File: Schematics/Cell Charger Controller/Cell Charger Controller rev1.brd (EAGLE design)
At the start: 177.8 x 114.3 mm, 54 parts, among them Q1 DMG3406L, U1 HM2102NLT

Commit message: charger controller board ready for review
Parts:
- added X1: CONNECTOR-4NANO-FIT-VERTICAL-4, HyTechDevices:1053101204
- moved C2 0.92 mm to (113.3, 79.0)
- moved R8 0.76 mm to (115.6, 26.2)
- moved C3 0.57 mm to (109.2, 79.0)
- moved U$5 0.57 mm to (119.4, 78.7)
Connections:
- net +12V: now also X1.1
- net ALERT_INA: now also U$2.A3
- net CANH: now also X1.4
- net CANL: now also X1.3
- net GND: now also X1.2
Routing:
- net ALERT_INA: track 0.00 -> 86.3 mm, vias 0 -> 2
- net +12V: track 18.0 -> 81.0 mm
- net CANL: track 0.00 -> 8.62 mm
- net CANH: track 0.00 -> 8.62 mm
- net +3V3: track 176.3 -> 178.2 mm
- net N$12: track 25.3 -> 26.7 mm
- net +5V: track 521.3 -> 522.6 mm
- net GND: track 151.5 -> 150.7 mm
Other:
- board text added: "10A Fuse"
- board text added: "2k"
- board text added: "5V Regulator"
- board text added: "CAN + 12V"
- board text added: "Cell Charger Controller rev 1 Designed by Leo Pozdneev"
- board text added: "GLV"
- board text added: "THERM1"
- board text added: "THERM2"
- board text added: "THERM3"
- board text added: "THERM4"
- board text added: "THERM5"
- board text added: "THERM6"
- board text added: "THERM7"
- board text added: "THERM8"
- board text added: "THERM9"
- board text added: "isoSPI"

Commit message: small changes to the controller board
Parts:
- removed R9: 0, HyTechDevices:0603-RES
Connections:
- removed net N$9: R9.2, U$4.12
- net N$12: no longer R9.1
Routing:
- net N$9: track 19.0 -> 0.00 mm
- net N$12: track 26.7 -> 12.6 mm, vias 1 -> 0
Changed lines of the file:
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@@
 <drawing>
 <settings>
-<setting alwaysvectorfont="yes"/>
+<setting alwaysvectorfont="no"/>
 <setting verticaltext="up"/>
 </settings>
@@
 <attribute name="VALUE" x="117.475" y="25.146" size="0.8128" layer="27" font="vector" rot="R90"/>
 </element>
-<element name="R9" library="HyTechDevices" package="0603-RES" value="0" x="148.844" y="74.168" smashed="yes">
-<attribute name="NAME" x="145.288" y="74.422" size="0.8128" layer="25" font="vector"/>
-<attribute name="VALUE" x="145.288" y="73.279" size="0.8128" layer="27" font="vector"/>
-</element>
 <element name="THERM1" library="HyTechDevices" package="1053091202" value="CONNECTOR-2NANO-FIT_VERTICAL-2" x="15.748" y="68.834" smashed="yes" rot="R270"/>
 <element name="THERM2" library="HyTechDevices" package="1053091202" value="CONNECTOR-2NANO-FIT_VERTICAL-2" x="15.748" y="61.214" smashed="yes" rot="R270"/>
@@
 <wire x1="158.496" y1="81.534" x2="158.496" y2="79.844" width="0.254" layer="1"/>
 </signal>
-<signal name="N$9">
-<contactref element="U$4" pad="12"/>
-<contactref element="R9" pad="2"/>
-<wire x1="159.1480125" y1="84.721" x2="158.6638" y2="84.721" width="0.254" layer="1"/>
-<wire x1="158.6638" y1="84.721" x2="158.6198" y2="84.765" width="0.254" layer="1"/>
-<wire x1="159.512" y1="84.3570125" x2="159.1480125" y2="84.721" width="0.254" layer="1"/>
-<wire x1="159.512" y1="77.7507875" x2="159.512" y2="84.3570125" width="0.254" layer="1"/>
-<wire x1="149.694" y1="74.168" x2="155.9292125" y2="74.168" width="0.254" layer="1"/>
-<wire x1="155.9292125" y1="74.168" x2="159.512" y2="77.7507875" width="0.254" layer="1"/>
-</signal>
 <signal name="ALERT_INA">
 <contactref element="U$4" pad="7"/>
@@
 <signal name="N$12">
 <contactref element="U$8" pad="S"/>
-<contactref element="R9" pad="1"/>
 <contactref element="U$4" pad="3"/>
 <contactref element="U$4" pad="1"/>
@@
 <wire x1="153.0842" y1="87.365" x2="153.0842" y2="86.715" width="0.508" layer="1"/>
 <wire x1="153.0842" y1="87.365" x2="153.0842" y2="86.065" width="0.508" layer="1"/>
-<via x="144.272" y="76.962" extent="1-16" drill="0.35"/>
-<wire x1="144.272" y1="86.2076" x2="144.272" y2="76.962" width="0.254" layer="16"/>
 <wire x1="144.272" y1="86.2076" x2="145.288" y2="87.2236" width="0.254" layer="16"/>
-<wire x1="147.994" y1="74.168" x2="147.066" y2="74.168" width="0.254" layer="1"/>
-<wire x1="144.272" y1="76.962" x2="147.066" y2="74.168" width="0.254" layer="1"/>
 </signal>
 <signal name="+12V">

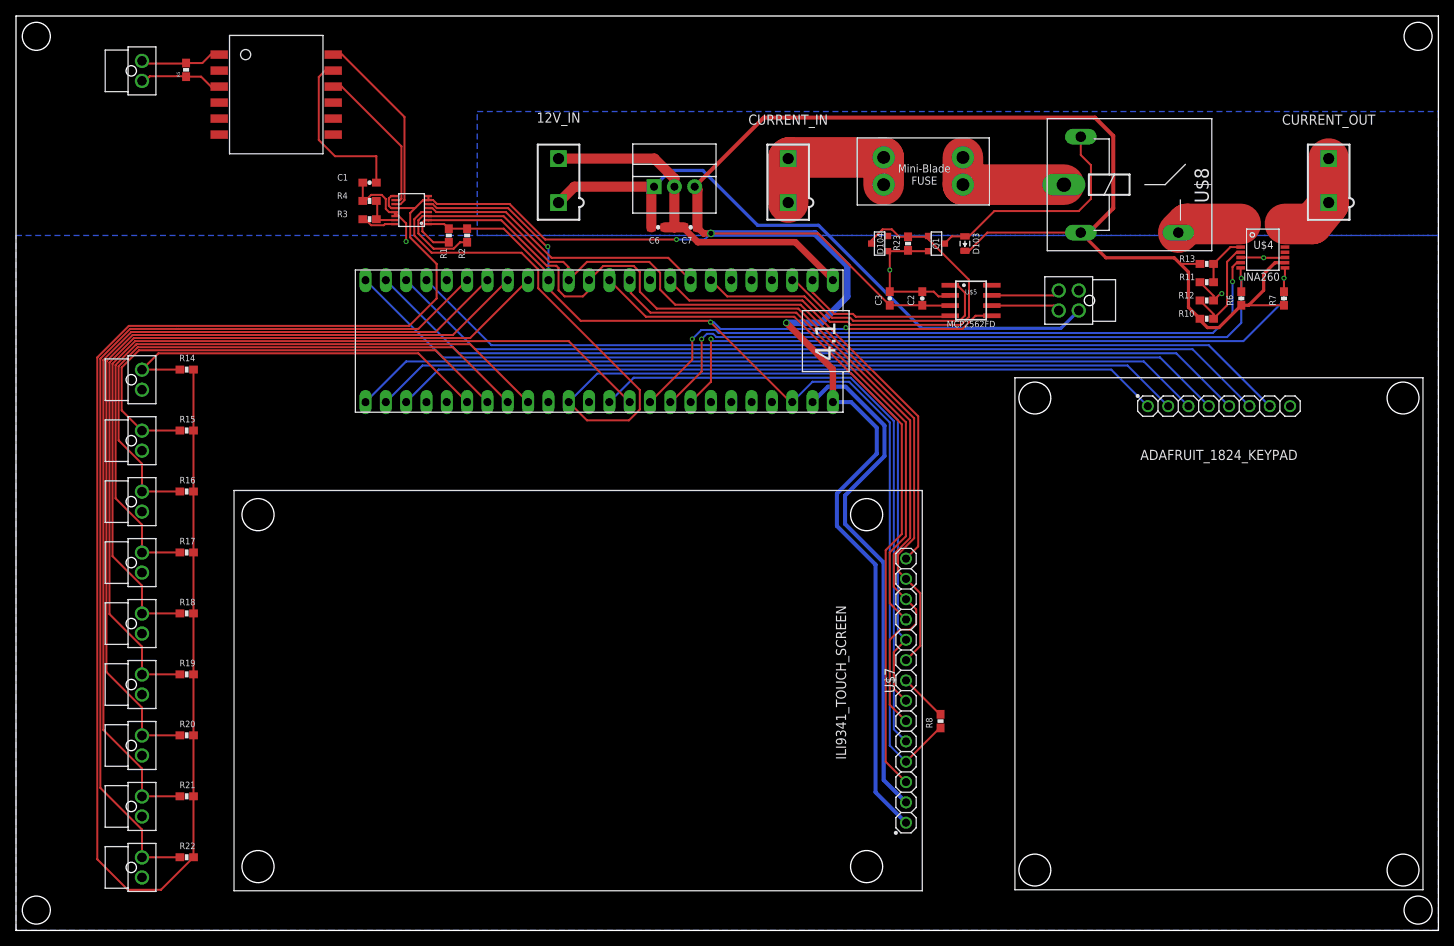
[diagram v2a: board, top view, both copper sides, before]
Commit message: generated gerbers for charger controller
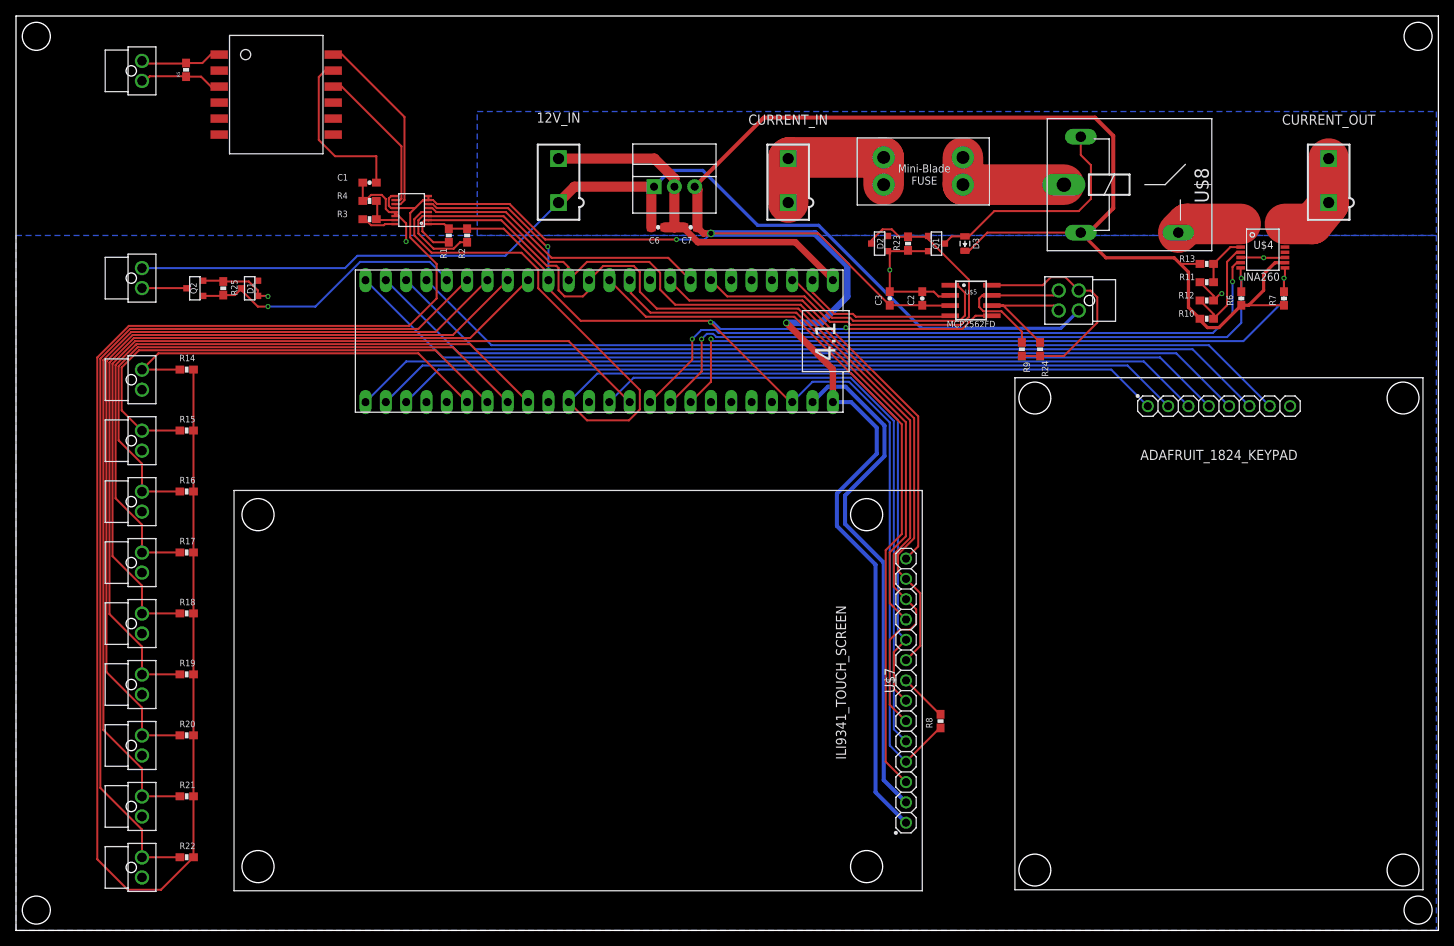
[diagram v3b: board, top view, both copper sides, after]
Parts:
- added BUZZER: CONNECTOR-2NANO-FIT_VERTICAL-2, HyTechDevices:1053091202
- added D1: MMBZ5246BLT1G, HyTechDevices:SOT23
- added Q2: DMG3406L, HyTechDevices:SOT23
- added R24, R9: 60, HyTechDevices:0603-RES
- added R25: 10k, HyTechDevices:0603-RES
- renumbered D103 to D3, D104 to D2
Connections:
- removed net N$8: U$5.8
- new net BUZZER_CTRL: D1.3, Q2.1, R25.2, U$2.D28
- new net N$16: BUZZER.2, Q2.3
- net +12V: now also BUZZER.1
- net CANH: now also R9.1
- net CANL: now also R24.2
- net GND: now also D1.1, Q2.2, R24.1, R25.1, R9.2, U$5.8
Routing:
- net +12V: track 81.0 -> 136.5 mm
- net GND: track 150.7 -> 189.1 mm, vias 4 -> 5
- net BUZZER_CTRL: track 0.00 -> 35.4 mm, vias 0 -> 1
- net CANH: track 8.62 -> 19.4 mm
- net CANL: track 8.62 -> 16.6 mm
- net N$16: track 0.00 -> 5.61 mm
- net N$12: track 12.6 -> 11.1 mm
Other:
- board text added: "BUZZER"
